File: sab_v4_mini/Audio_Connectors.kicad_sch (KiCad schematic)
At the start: 8 parts, among them J12 AudioJack_LOOP2_RETURN, J13 AudioJack_LOOP3_RETURN, J14 AudioJack_INPUT, J15 AudioJack_LOOP1_SEND, J16 AudioJack_LOOP2_SEND, J7 AudioJack_LOOP1_RETURN, J8 AudioJack_LOOP3_SEND, J9 AudioJack_OUTPUT

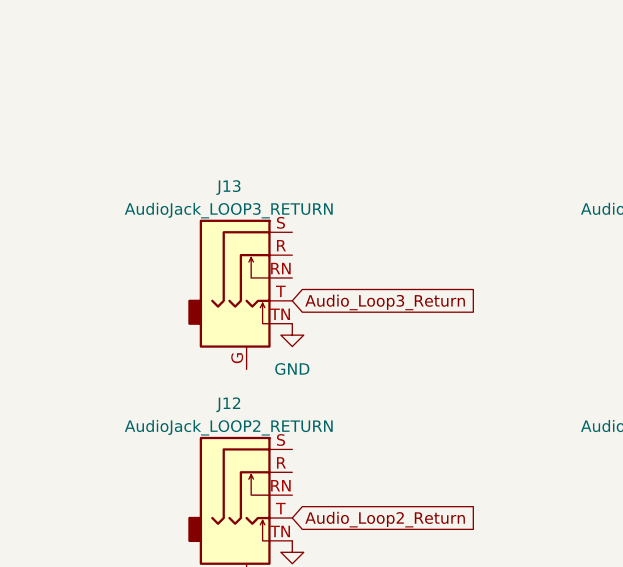
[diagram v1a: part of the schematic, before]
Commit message: added codec
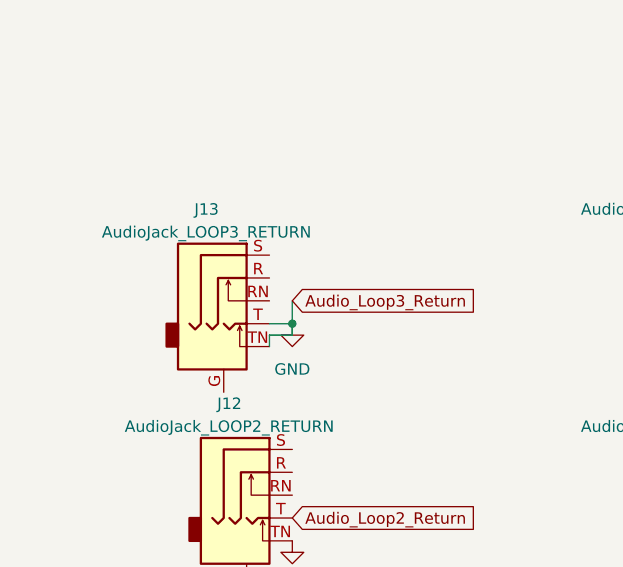
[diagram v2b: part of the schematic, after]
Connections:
- net Audio_Loop3_Return is gone; now on net GND: J13.T
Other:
- moved on the sheet: J13
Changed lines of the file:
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@@
 	(generator_version "8.0")
 	(paper "A4")
+	(junction
+		(at 48.26 105.41)
+		(diameter 0)
+		(color 0 0 0 0)
+	)
+	(wire
+		(pts
+			(xy 45.72 105.41) (xy 48.26 105.41)
+		)
+		(stroke
+			(width 0)
+			(type default)
+		)
+	)
+	(wire
+		(pts
+			(xy 45.72 107.95) (xy 45.72 106.68)
+		)
+		(stroke
+			(width 0)
+			(type default)
+		)
+	)
 	(wire
 		(pts
@@
 		(pts
 			(xy 97.79 43.18) (xy 95.25 43.18)
+		)
+		(stroke
+			(width 0)
+			(type default)
+		)
+	)
+	(wire
+		(pts
+			(xy 48.26 106.68) (xy 48.26 105.41)
+		)
+		(stroke
+			(width 0)
+			(type default)
+		)
+	)
+	(wire
+		(pts
+			(xy 45.72 106.68) (xy 48.26 106.68)
+		)
+		(stroke
+			(width 0)
+			(type default)
+		)
+	)
+	(wire
+		(pts
+			(xy 48.26 105.41) (xy 48.26 102.87)
 		)
 		(stroke
@@
 	(symbol
 		(lib_id "Connector_Audio:AudioJack3_Ground_SwitchTR")
-		(at 43.18 97.79 0)
+		(at 40.64 100.33 0)
 		(unit 1)
 		(exclude_from_sim no)
@@
 		(fields_autoplaced yes)
 		(property "Reference" "J13"
-			(at 41.275 90.17 0)
+			(at 38.735 92.71 0)
 			(effects
 				(font
@@
 		)
 		(property "Value" "AudioJack_LOOP3_RETURN"
-			(at 41.275 92.71 0)
+			(at 38.735 95.25 0)
 			(effects
 				(font
@@
 		)
 		(property "Footprint" "stm_audio_board_footprints:6.3_jack_new_ref"
-			(at 43.18 97.79 0)
+			(at 40.64 100.33 0)
 			(effects
 				(font
@@
 		)
 		(property "Datasheet" "~"
-			(at 43.18 97.79 0)
+			(at 40.64 100.33 0)
 			(effects
 				(font
@@
 		)
 		(property "Description" ""
-			(at 43.18 97.79 0)
+			(at 40.64 100.33 0)
 			(effects
 				(font
@@
 		)
 		(property "LCSC Part" "C309277"
-			(at 43.18 97.79 0)
-			(effects
-				(font
+			(at 40.64 100.33 0)
+			(effects
+				(font
